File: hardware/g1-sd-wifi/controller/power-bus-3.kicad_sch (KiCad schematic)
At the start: 45 parts, among them U35 SN74LVC16T245, U36 SN74LVC244A host controls, U37 SN74LVC1G17 host RESETn, U38 SN74LVC1G125 qualified ATA_IN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, U39 SN74LVC1G125 qualified ATA_DM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, U70 SN74LVC1G07 open-drain IORDY, U71 TPS22919 Wi-Fi input switch, U72 SN74LVC1G32DBVR, U73 SN74LVC1G32DBVR

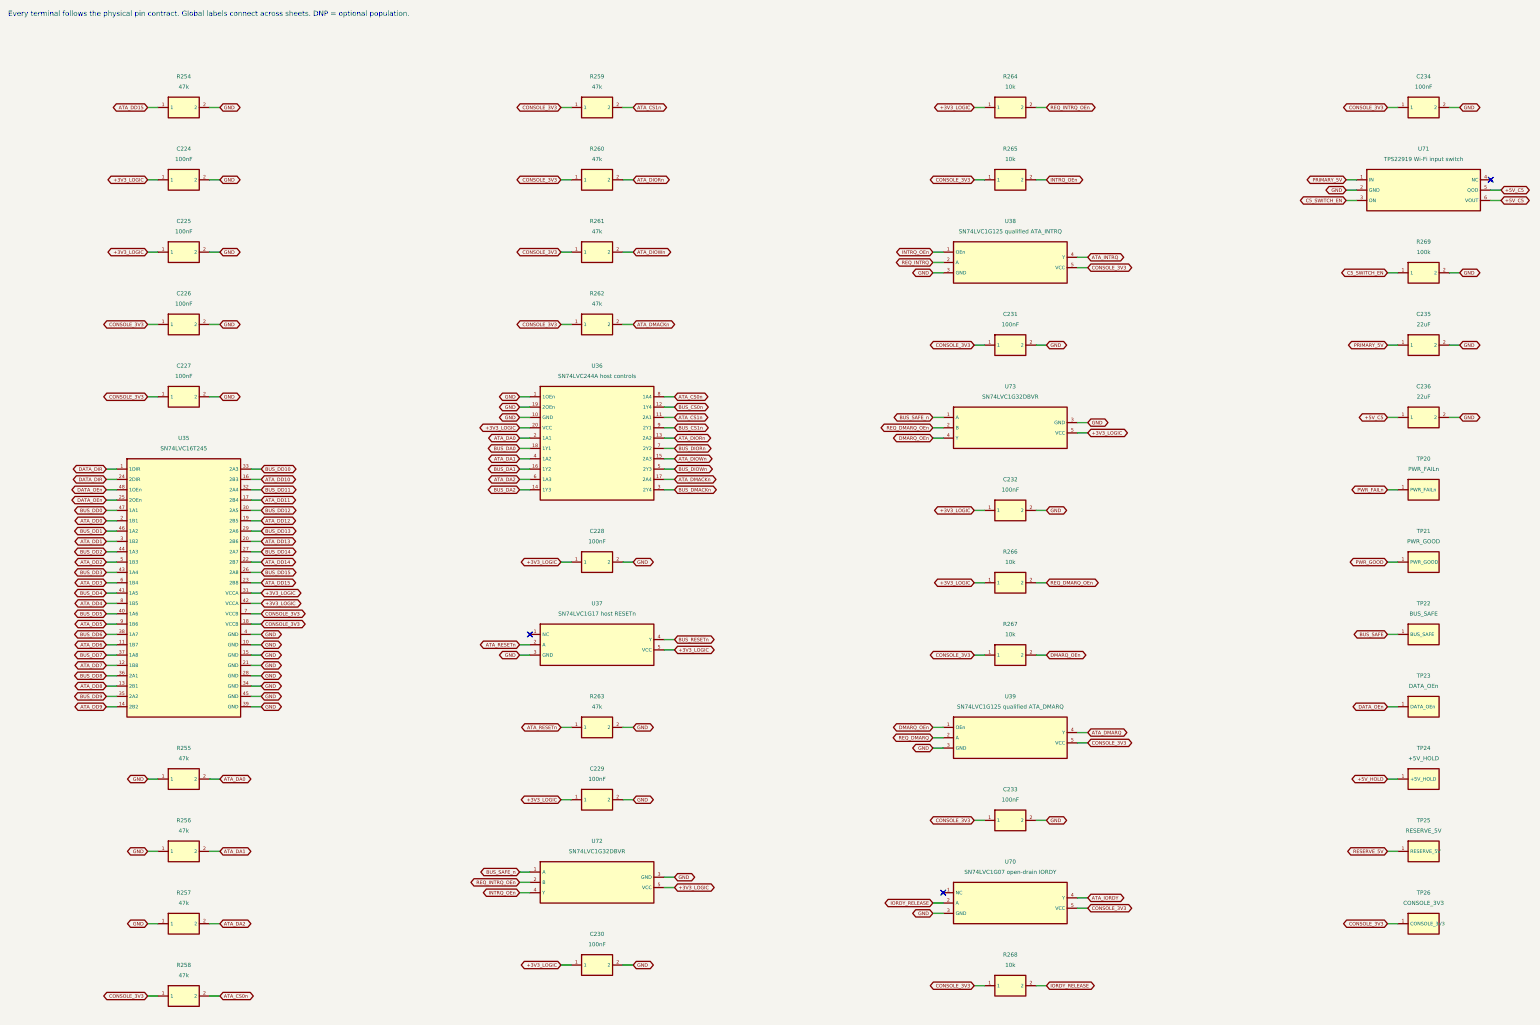
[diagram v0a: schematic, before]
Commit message: G1 carrier: FPGA pull-downs replace the sixteen BUS_DD biases
The 47 k biases on BUS_DD (between the FPGA and U35's A port) found no
room near that bus and were placed up to 40 mm away; their connections
were a quarter of what the router could not close. The FPGA's own I/O
pull-down now holds BUS_DD during tri-state idle (PULLMODE=DOWN in the
LPF, emitted by sync_fpga_pins.py). Before configuration U35 is held
disabled by its DATA_OEn pull-up; the MachXO2's unconfigured pin state
is to be confirmed against Lattice TN1202 at bring-up. The host-side
ATA_DD biases stay.

- power-bus.json drops R223..R253 (odd); integration counts 349/360/351;
  ERC 0; integration audit passes; parts list BASE 263 fitted parts.
- update_board_from_netlist: --allow-remove deletes a removed part's
  footprint and pad copper.
- floorplan script: removes the biases and places the optional reserve
  bank (C202-C205) beside U20, which it feeds, instead of 90 mm away.
- Board regenerated: 153/153 placed, native DRC 0, parity 0. Routing in
  progress.

Co-Authored-By: Claude Opus 5.5 <noreply@anthropic.com>
Claude-Session: https://claude.ai/code/session_01Gp9EYc2r9fMpZ7V8WtfonZ
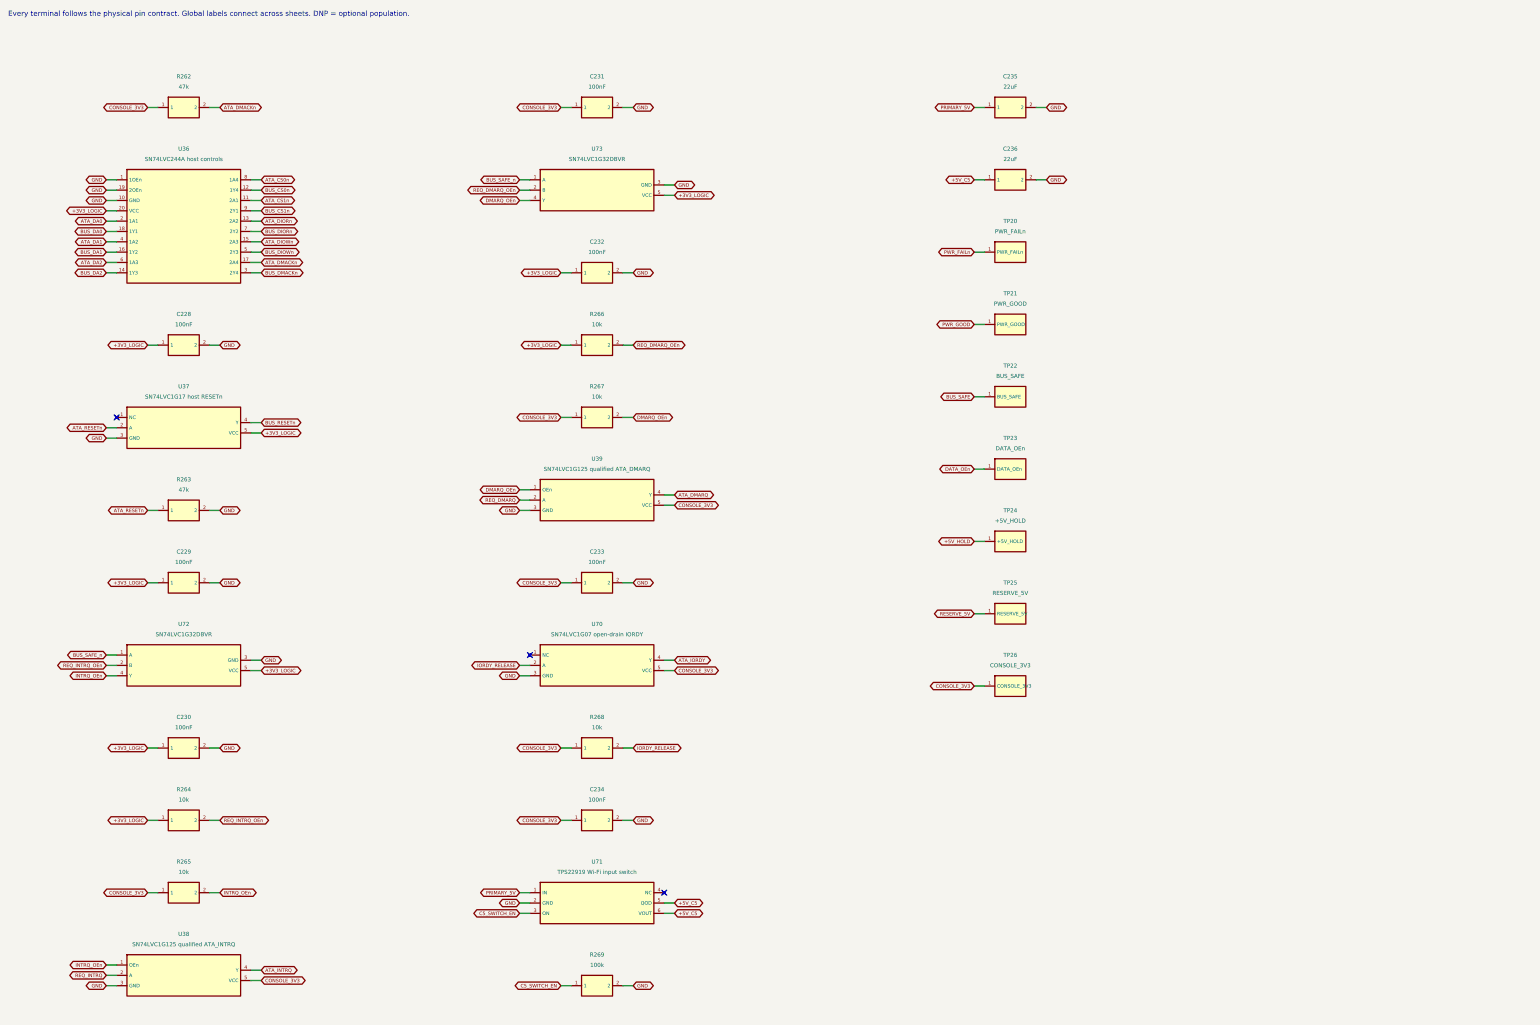
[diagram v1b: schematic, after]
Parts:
- removed C224: 100nF, KUI_Footprints:C_0402_1005Metric, symbol KUI_G1:C224
- removed C225: 100nF, KUI_Footprints:C_0402_1005Metric, symbol KUI_G1:C225
- removed C226: 100nF, KUI_Footprints:C_0402_1005Metric, symbol KUI_G1:C226
- removed C227: 100nF, KUI_Footprints:C_0402_1005Metric, symbol KUI_G1:C227
- removed R254: 47k, KUI_Footprints:R_0402_1005Metric, symbol KUI_G1:R254
- removed R255: 47k, KUI_Footprints:R_0402_1005Metric, symbol KUI_G1:R255
- removed R256: 47k, KUI_Footprints:R_0402_1005Metric, symbol KUI_G1:R256
- removed R257: 47k, KUI_Footprints:R_0402_1005Metric, symbol KUI_G1:R257
- removed R258: 47k, KUI_Footprints:R_0402_1005Metric, symbol KUI_G1:R258
- removed R259: 47k, KUI_Footprints:R_0402_1005Metric, symbol KUI_G1:R259
- removed R260: 47k, KUI_Footprints:R_0402_1005Metric, symbol KUI_G1:R260
- removed R261: 47k, KUI_Footprints:R_0402_1005Metric, symbol KUI_G1:R261
- removed U35: SN74LVC16T245, KUI_Footprints:TSSOP-48_6.1x12.5mm_P0.5mm, symbol KUI_G1:U35
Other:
- moved on the sheet: C228, C229, C230, C231, C232, C233, C234, C235, C236, R262, R263, R264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

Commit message: G1 carrier: D21 input TVS turns a 12-V mis-wire into a blown F20
A bidirectional 5-V TVS (SMF5.0CA, SOD-123FL) from FUSED_5V to GND,
between F20 and Q20: above about 6.4 V it conducts far more than F20's
1.5 A rating, so a wrong 12-V feed opens the fuse instead of sitting on
the 5-V parts. Bidirectional, so a reversed 5-V feed stays below
breakdown and Q20 blocks it without blowing F20. Downstream parts may
still see the ~9 V clamp while F20 clears; the doc says so.

Schematic, netlist, ERC (0), integration audit (361 parts) and parts
list regenerated. Its datasheet and JLC catalog identity could not be
reached from this environment, so the part is listed sourcing-pending.
The floorplan places D21 2.2 mm from F20's output; the netlist updater
can now add a part whose footprint is not on the board yet. The power
doc also notes that F20 does not protect the harness itself.

Co-Authored-By: Claude Opus 5.5 <noreply@anthropic.com>
Claude-Session: https://claude.ai/code/session_01Gp9EYc2r9fMpZ7V8WtfonZ
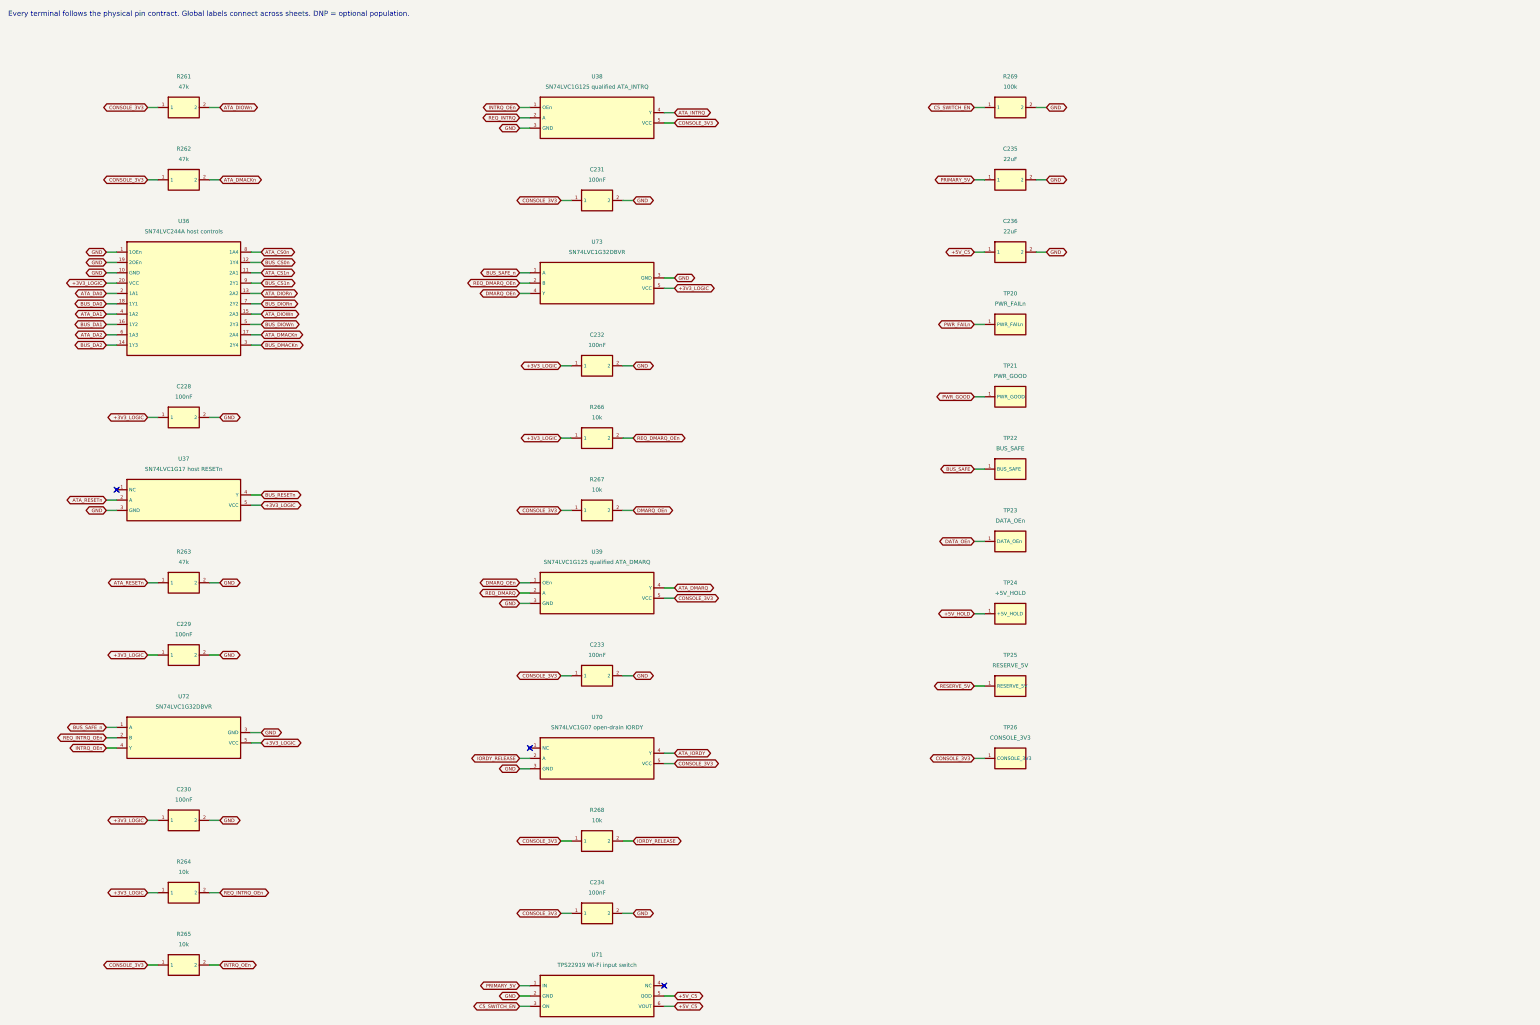
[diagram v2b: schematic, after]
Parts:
- added R261: 47k, KUI_Footprints:R_0402_1005Metric, symbol KUI_G1:R261
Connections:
- net ATA_DIOWn: now also R261.2
- net CONSOLE_3V3: now also R261.1
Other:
- moved on the sheet: C228, C229, C230, C231, C232, C233, C234, C235, C236, R262, R263, R264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

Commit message: G1 safety: fuse the host 3.3-V entry; no console 5 V on the flex or carrier
Host 3.3 V reached about 30 carrier parts straight from two flex contacts,
and the two console-5-V contacts were joined by an unused carrier trace;
a short on either would load a console supply through 0.5 A connector
contacts with no fuse anywhere. Now:

- F21 (0467.500NR, 0.5 A fast, same 467 family as F20) sits between the one
  remaining 3.3-V entry, J51 B1, and CONSOLE_3V3. If it opens the buffers
  lose VCCB and isolate, and U25 reports the host rail absent.
- CN503 A1 (second 3.3 V) and A3/B3 (5 V) get no flex copper at all: no
  landing pad, no trace, only an unconnected mating finger, so a chafed
  flex cannot short a console supply. Their carrier socket pins are bare.
  flex-interface.json lists them; the flex and carrier generators and both
  checks read that list. Flex ERC/DRC/parity 0; carrier ERC 0, integration
  check pass (362 parts).
- The DSN export keeps the 5-V and storage supply nets on the 1 oz outer
  layers: on 0.5 oz inner copper a 0.25 mm track at the fuse current would
  overheat (IPC-2221).
- F21 is placed by the floorplan next to J51; board DRC 0, parity 0
  (unrouted).

Co-Authored-By: Claude Opus 5.5 <noreply@anthropic.com>
Claude-Session: https://claude.ai/code/session_01Gp9EYc2r9fMpZ7V8WtfonZ
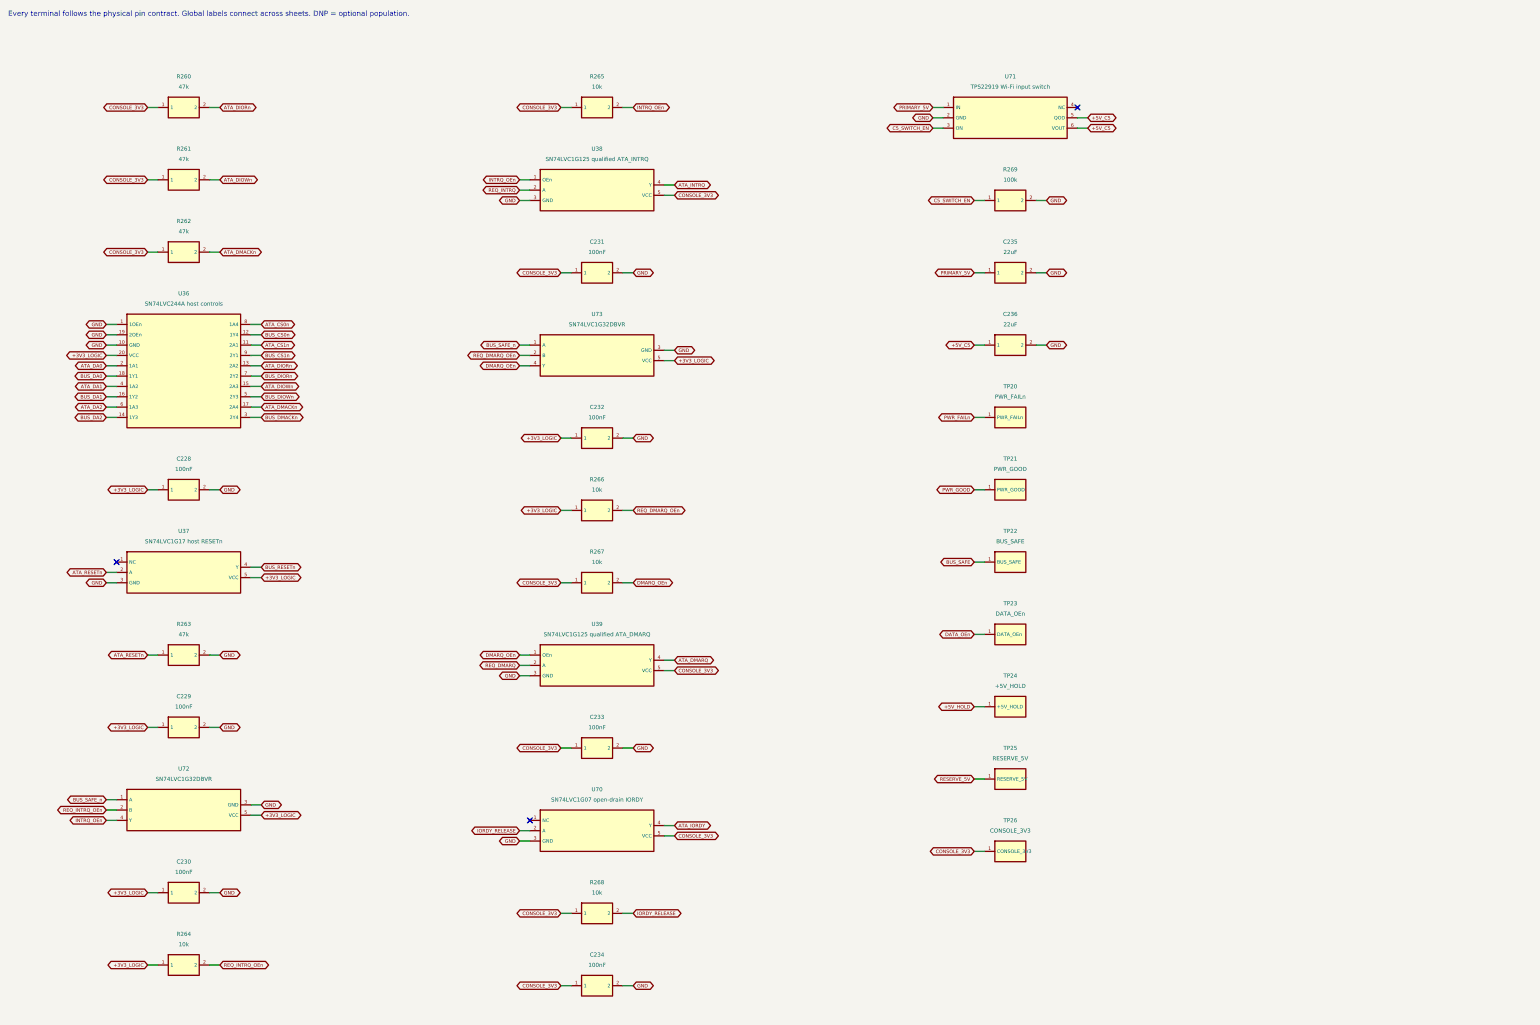
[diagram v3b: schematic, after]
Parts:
- added R260: 47k, KUI_Footprints:R_0402_1005Metric, symbol KUI_G1:R260
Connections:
- net ATA_DIORn: now also R260.2
- net CONSOLE_3V3: now also R260.1
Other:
- moved on the sheet: C228, C229, C230, C231, C232, C233, C234, C235, C236, R261, R262, R263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
